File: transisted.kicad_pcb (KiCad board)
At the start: 2 copper layers, 96.2 x 99.1 mm, 12 parts, among them Q1 NPN, Q2 NPN, SW1 SW_Push, SW2 SW_Push

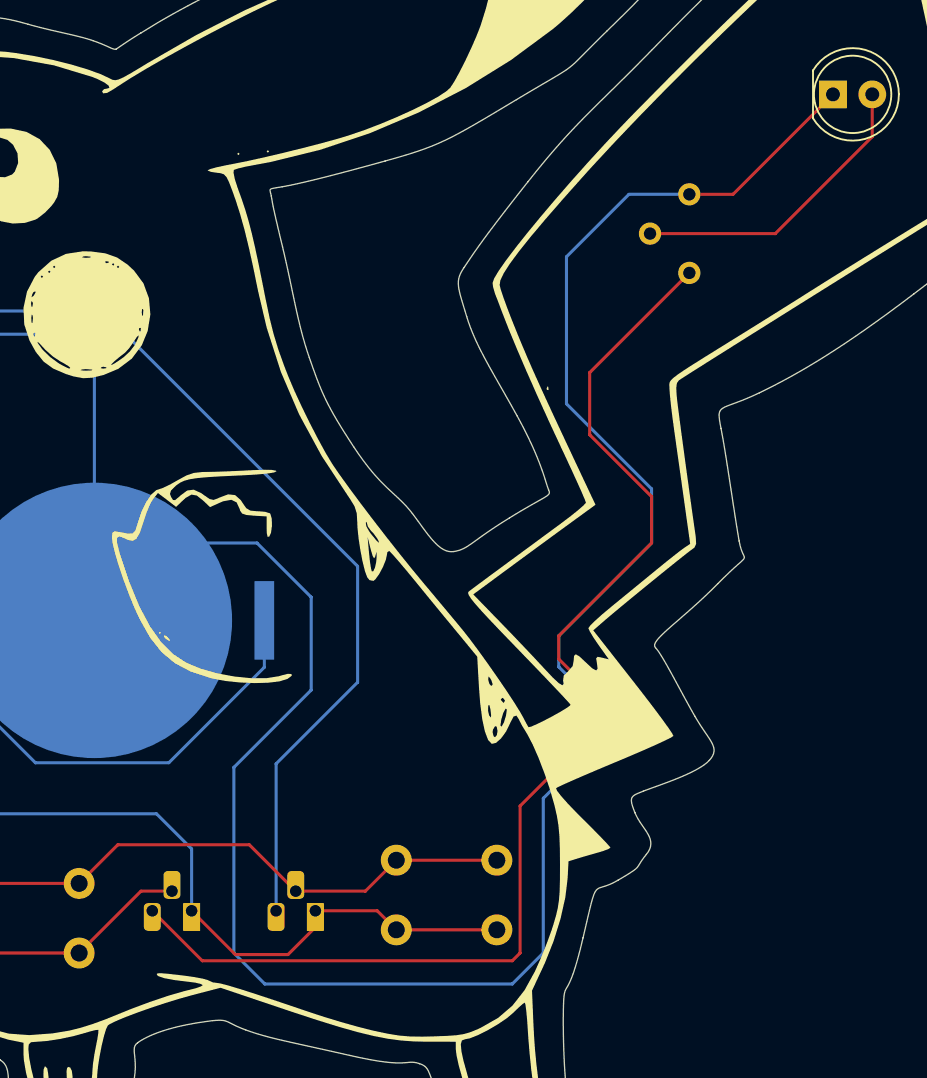
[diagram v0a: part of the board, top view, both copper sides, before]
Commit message: Removed an unnecessary trace
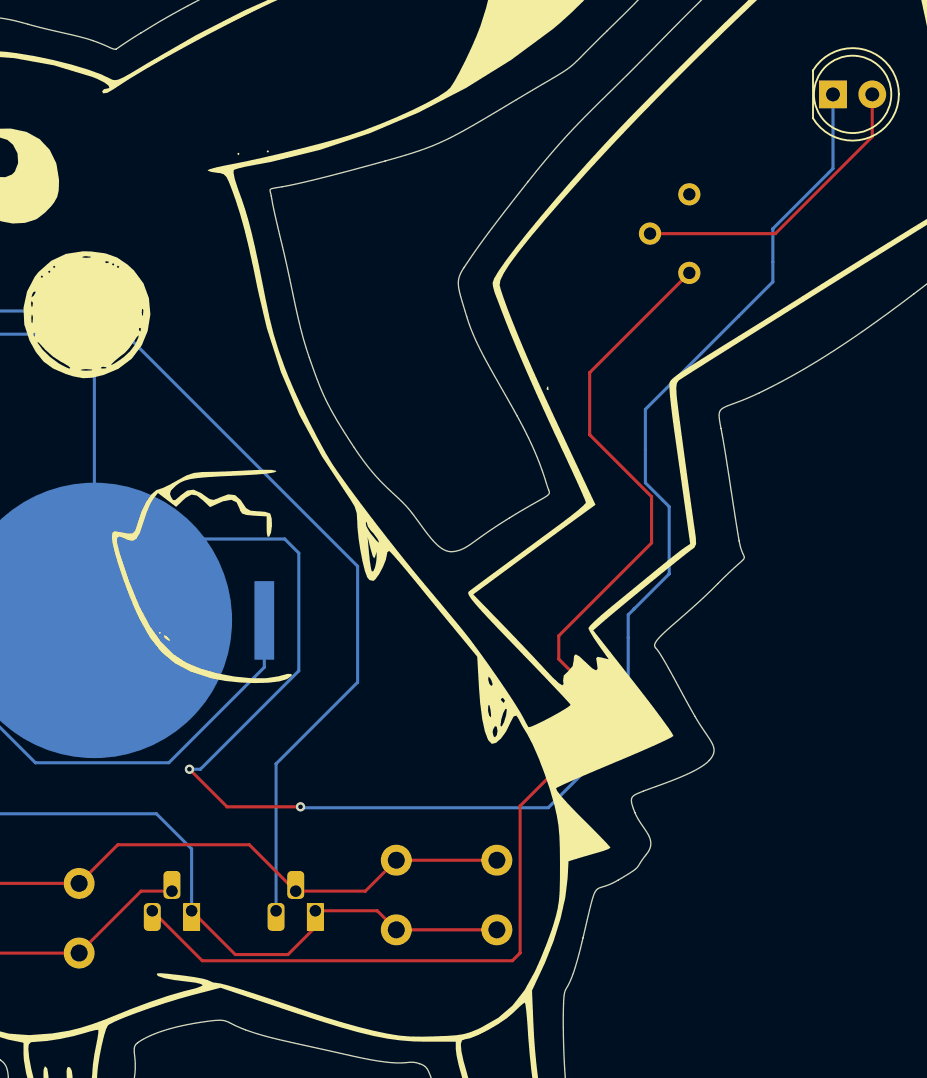
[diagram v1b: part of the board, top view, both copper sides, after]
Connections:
- RV1 pad 3: Net-(BT1--) -> unconnected-(RV1-Pad3)
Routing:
- net Net-(BT1--): track 185.5 -> 159.4 mm, vias 2 -> 4
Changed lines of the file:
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@@
 	(net 7 "Net-(Q2-B)")
 	(net 8 "Net-(Q2-E)")
+	(net 9 "unconnected-(RV1-Pad3)")
 	(footprint "LED_THT:LED_D5.0mm"
 		(layer "F.Cu")
@@
 			(layers "*.Cu" "*.Mask")
 			(remove_unused_layers no)
-			(net 1 "Net-(BT1--)")
+			(net 9 "unconnected-(RV1-Pad3)")
 			(pinfunction "3")
 			(pintype "passive")
@@
 	)
 	(segment
-		(start 116.44 58.96)
-		(end 119.265 58.96)
+		(start 91.31 98.55)
+		(end 86.56 98.55)
 		(width 0.2)
 		(layer "F.Cu")
@@
 	)
 	(segment
-		(start 119.265 58.96)
-		(end 125.725 52.5)
+		(start 75.96 66.96)
+		(end 75.96 66.5)
 		(width 0.2)
 		(layer "F.Cu")
@@
 	)
 	(segment
-		(start 75.96 66.96)
-		(end 75.96 66.5)
+		(start 51.225 69.5)
+		(end 51.225 69.275)
 		(width 0.2)
 		(layer "F.Cu")
@@
 	)
 	(segment
-		(start 51.225 69.5)
-		(end 51.225 69.275)
+		(start 86.56 98.55)
+		(end 84.13 96.12)
 		(width 0.2)
 		(layer "F.Cu")
@@
 	)
 	(via
+		(at 91.31 98.55)
+		(size 0.6)
+		(drill 0.3)
+		(layers "F.Cu" "B.Cu")
+		(net 1)
+	)
+	(via
 		(at 78 69)
 		(size 0.6)
@@
 	)
 	(via
+		(at 84.13 96.12)
+		(size 0.6)
+		(drill 0.3)
+		(layers "F.Cu" "B.Cu")
+		(net 1)
+	)
+	(via
 		(at 52 68.5)
 		(size 0.6)
@@
 	)
 	(segment
-		(start 108 89.5)
-		(end 111 92.5)
+		(start 77.985 86.5)
+		(end 77.985 69.015)
 		(width 0.2)
 		(layer "B.Cu")
@@
 	)
 	(segment
-		(start 77.985 86.5)
-		(end 77.985 69.015)
+		(start 90.29 81.24)
+		(end 83.245 81.24)
 		(width 0.2)
 		(layer "B.Cu")
@@
 	)
 	(segment
-		(start 116.44 58.96)
-		(end 112.54 58.96)
+		(start 114.71 78.72)
+		(end 115.14 79.15)
 		(width 0.2)
 		(layer "B.Cu")
@@
 	)
 	(segment
-		(start 108.5 72.5)
-		(end 114 78)
+		(start 107.74 98.19)
+		(end 107.32 98.61)
 		(width 0.2)
 		(layer "B.Cu")
@@
 	)
 	(segment
-		(start 82.985 81.5)
-		(end 77.985 86.5)
+		(start 115.14 83.49)
+		(end 112.88 85.75)
 		(width 0.2)
 		(layer "B.Cu")
@@
 	)
 	(segment
-		(start 112.54 58.96)
-		(end 108.5 63)
+		(start 112.49 93.71)
+		(end 112.36 93.84)
 		(width 0.2)
 		(layer "B.Cu")
@@
 	)
 	(segment
-		(start 87 108)
-		(end 87 96)
+		(start 125.44 57.58)
+		(end 121.84 61.18)
 		(width 0.2)
 		(layer "B.Cu")
@@
 	)
 	(segment
-		(start 89 110)
-		(end 87 108)
+		(start 91.37 98.61)
+		(end 91.31 98.55)
 		(width 0.2)
 		(layer "B.Cu")
@@
 	)
 	(segment
+		(start 107.32 98.61)
+		(end 91.37 98.61)
+		(width 0.2)
+		(layer "B.Cu")
+		(net 1)
+	)
+	(segment
 		(start 77.985 69.015)
 		(end 78 69)
@@
 	)
 	(segment
-		(start 88.5 81.5)
-		(end 82.985 81.5)
+		(start 112.09 93.84)
+		(end 107.74 98.19)
+		(width 0.2)
+		(layer "B.Cu")
+		(net 1)
+	)
+	(segment
+		(start 113.6 75.45)
+		(end 113.6 77.61)
 		(width 0.2)
 		(layer "B.Cu")
@@
 	)
 	(segment
-		(start 107 98)
-		(end 107 108)
+		(start 121.84 64.62)
+		(end 119.62 66.84)
 		(width 0.2)
 		(layer "B.Cu")
@@
 	)
 	(segment
-		(start 107 108)
-		(end 105 110)
+		(start 121.84 63.34)
+		(end 121.84 64.62)
 		(width 0.2)
 		(layer "B.Cu")
@@
 	)
 	(segment
-		(start 92 91)
-		(end 92 85)
+		(start 119.62 66.84)
+		(end 113.6 72.86)
 		(width 0.2)
 		(layer "B.Cu")
@@
 	)
 	(segment
-		(start 87 96)
-		(end 92 91)
+		(start 121.84 61.18)
+		(end 121.84 63.34)
 		(width 0.2)
 		(layer "B.Cu")
@@
 	)
 	(segment
-		(start 111 94)
-		(end 107 98)
+		(start 91.2 89.76)
+		(end 91.2 82.15)
 		(width 0.2)
 		(layer "B.Cu")
@@
 	)
 	(segment
-		(start 114 81.5)
-		(end 108 87.5)
+		(start 112.49 86.14)
+		(end 112.49 87.62)
 		(width 0.2)
 		(layer "B.Cu")
@@
 	)
 	(segment
-		(start 114 78)
-		(end 114 81.5)
+		(start 115.14 79.15)
+		(end 115.14 82.65)
 		(width 0.2)
 		(layer "B.Cu")
@@
 	)
 	(segment
-		(start 92 85)
-		(end 88.5 81.5)
+		(start 112.36 93.84)
+		(end 112.09 93.84)
 		(width 0.2)
 		(layer "B.Cu")
@@
 	)
 	(segment
-		(start 108 87.5)
-		(end 108 89.5)
+		(start 84.84 96.12)
+		(end 91.2 89.76)
+		(width 0.2)
+		(layer "B.Cu")
+		(net 1)
+	)
+	(segment
+		(start 125.725 52.5)
+		(end 125.725 57.295)
+		(width 0.2)
+		(layer "B.Cu")
+		(net 1)
+	)
+	(segment
+		(start 115.14 82.65)
+		(end 115.14 83.49)
+		(width 0.2)
+		(layer "B.Cu")
+		(net 1)
+	)
+	(segment
+		(start 112.49 87.62)
+		(end 112.49 93.71)
+		(width 0.2)
+		(layer "B.Cu")
+		(net 1)
+	)
+	(segment
+		(start 84.13 96.12)
+		(end 84.84 96.12)
+		(width 0.2)
+		(layer "B.Cu")
+		(net 1)
+	)
+	(segment
+		(start 83.245 81.24)
+		(end 77.985 86.5)
 		(width 0.2)
 		(layer "B.Cu")
@@
 	)
 	(segment
-		(start 105 110)
-		(end 89 110)
+		(start 91.2 82.15)
+		(end 90.29 81.24)
+		(width 0.2)
+		(layer "B.Cu")
+		(net 1)
+	)
+	(segment
+		(start 112.88 85.75)
+		(end 112.49 86.14)
+		(width 0.2)
+		(layer "B.Cu")
+		(net 1)
+	)
+	(segment
+		(start 113.6 77.61)
+		(end 114.71 78.72)
 		(width 0.2)
 		(layer "B.Cu")
@@
 	)
 	(segment
-		(start 108.5 63)
-		(end 108.5 72.5)
+		(start 125.725 57.295)
+		(end 125.44 57.58)
 		(width 0.2)
 		(layer "B.Cu")
@@
 	)
 	(segment
-		(start 111 92.5)
-		(end 111 94)
+		(start 113.6 72.86)
+		(end 113.6 75.45)
 		(width 0.2)
 		(layer "B.Cu")
